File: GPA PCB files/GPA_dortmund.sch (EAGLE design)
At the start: 164 parts, among them U10 INA149SOIC8, U100 AAVID_TO220_HEATSINK, U101 AAVID_TO220_HEATSINK, U102 AAVID_TO220_HEATSINK, U103 AAVID_TO220_HEATSINK, U11 OPA549_KV_11TO-220_11, U12 OPA549_KV_11TO-220_11, U13 INA149SOIC8, U17 OPA549_KV_11TO-220_11, U18 OPA549_KV_11TO-220_11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

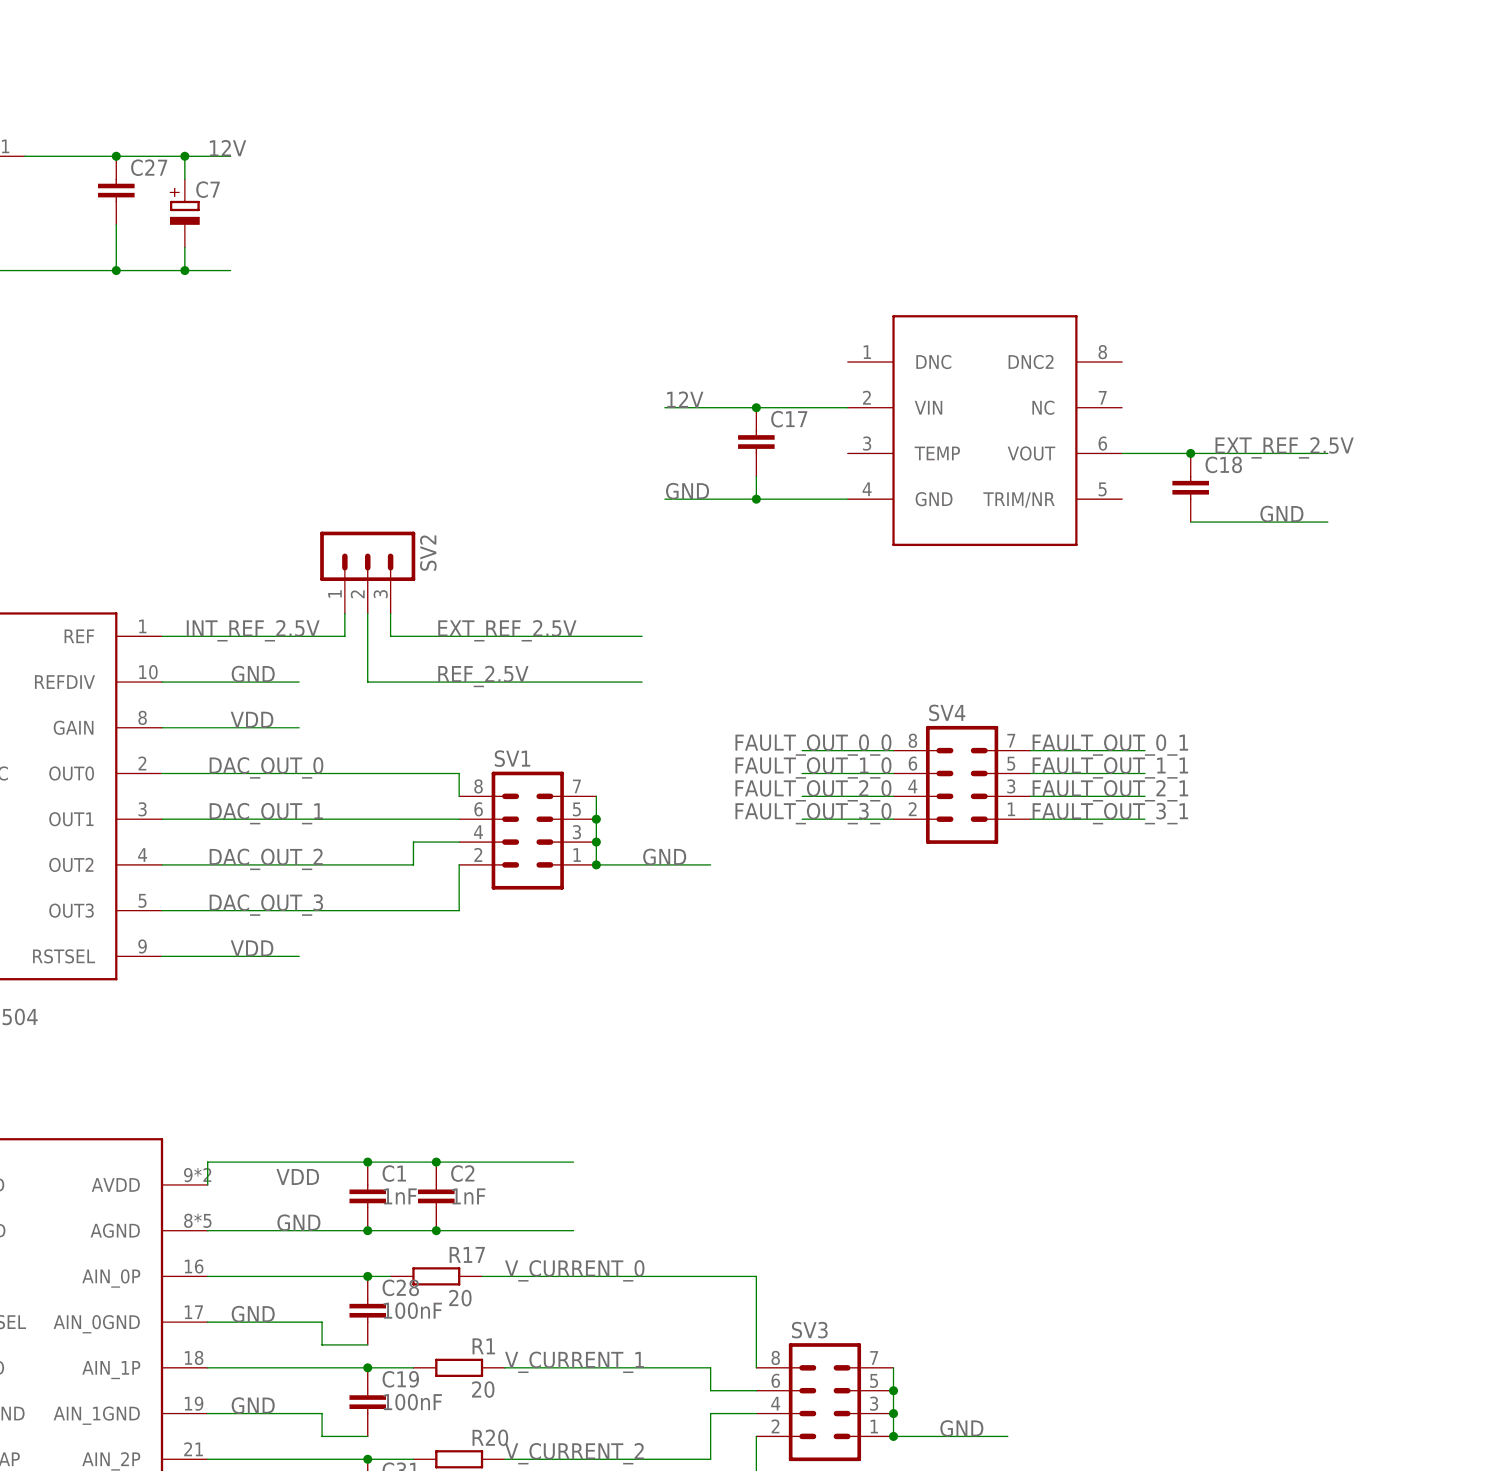
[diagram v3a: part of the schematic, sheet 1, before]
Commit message: added jumpers for switching between analog and digital input
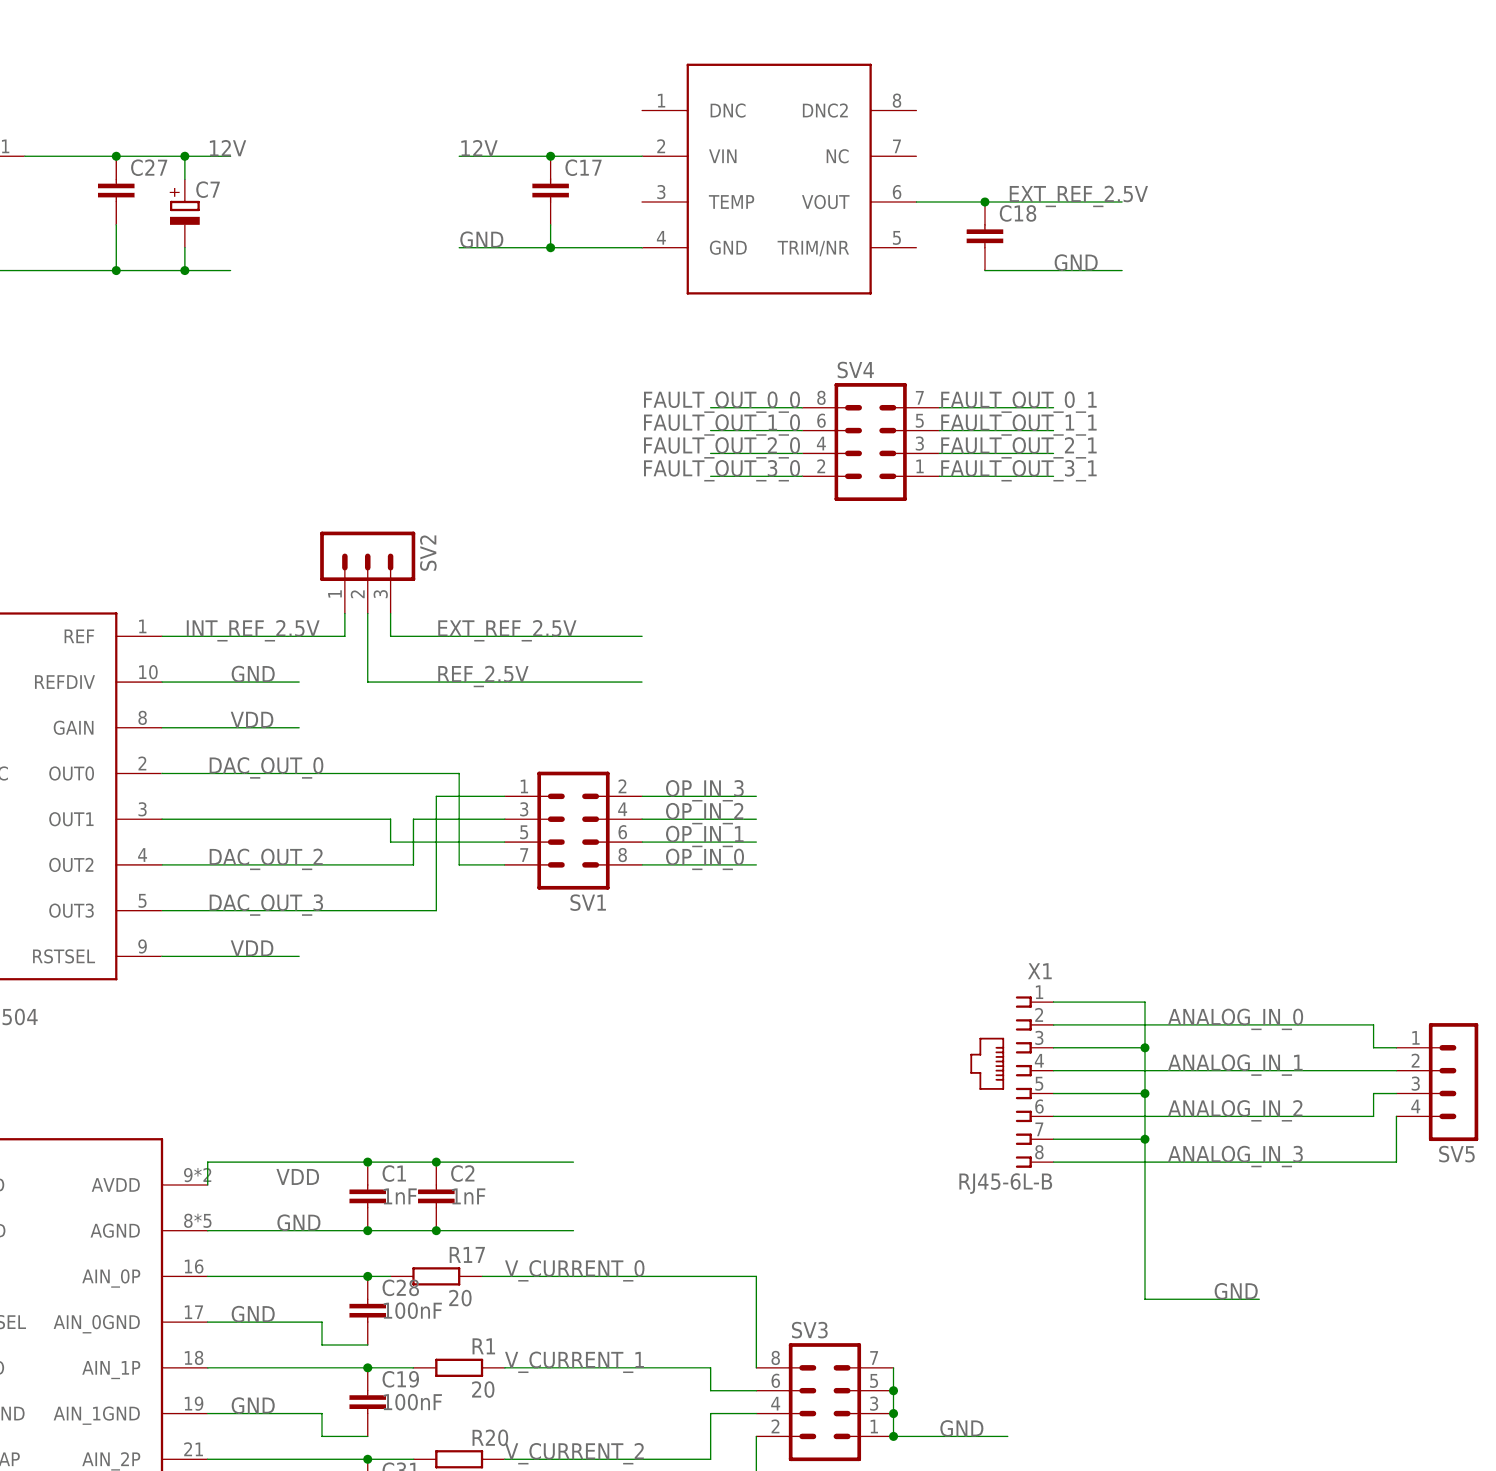
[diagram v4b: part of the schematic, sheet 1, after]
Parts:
- added SV5: (no value), my_parts:MA04-1_SLIM
- added X1: RJ45-6L-B, con-tycoelectronics:RJ45-6L-B
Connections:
- removed net DAC_OUT_1: R70.2, SV1.6, U6.OUT1
- new net ANALOG_IN_0: SV5.1, X1.2
- new net ANALOG_IN_1: SV5.2, X1.4
- new net ANALOG_IN_2: SV5.3, X1.6
- new net ANALOG_IN_3: SV5.4, X1.8
- new net N$3: SV1.5, U6.OUT1
- new net OP_IN_0: R98.2, SV1.8
- new net OP_IN_1: R70.2, SV1.6
- new net OP_IN_2: R28.2, SV1.4
- new net OP_IN_3: R42.2, SV1.2
- net DAC_OUT_0: now also SV1.7; no longer R98.2, SV1.8
- net DAC_OUT_2: now also SV1.3; no longer R28.2, SV1.4
- net DAC_OUT_3: now also SV1.1; no longer R42.2, SV1.2
- net GND: now also X1.1, X1.3, X1.5, X1.7; no longer SV1.1, SV1.3, SV1.5, SV1.7
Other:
- moved on the sheet: C17, C18, SV1, SV4

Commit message: Revert "added jumpers for switching between analog and digital input"
This reverts commit bcba1545b7b5a1e681abaa340a80f0f9e8fd90d3.
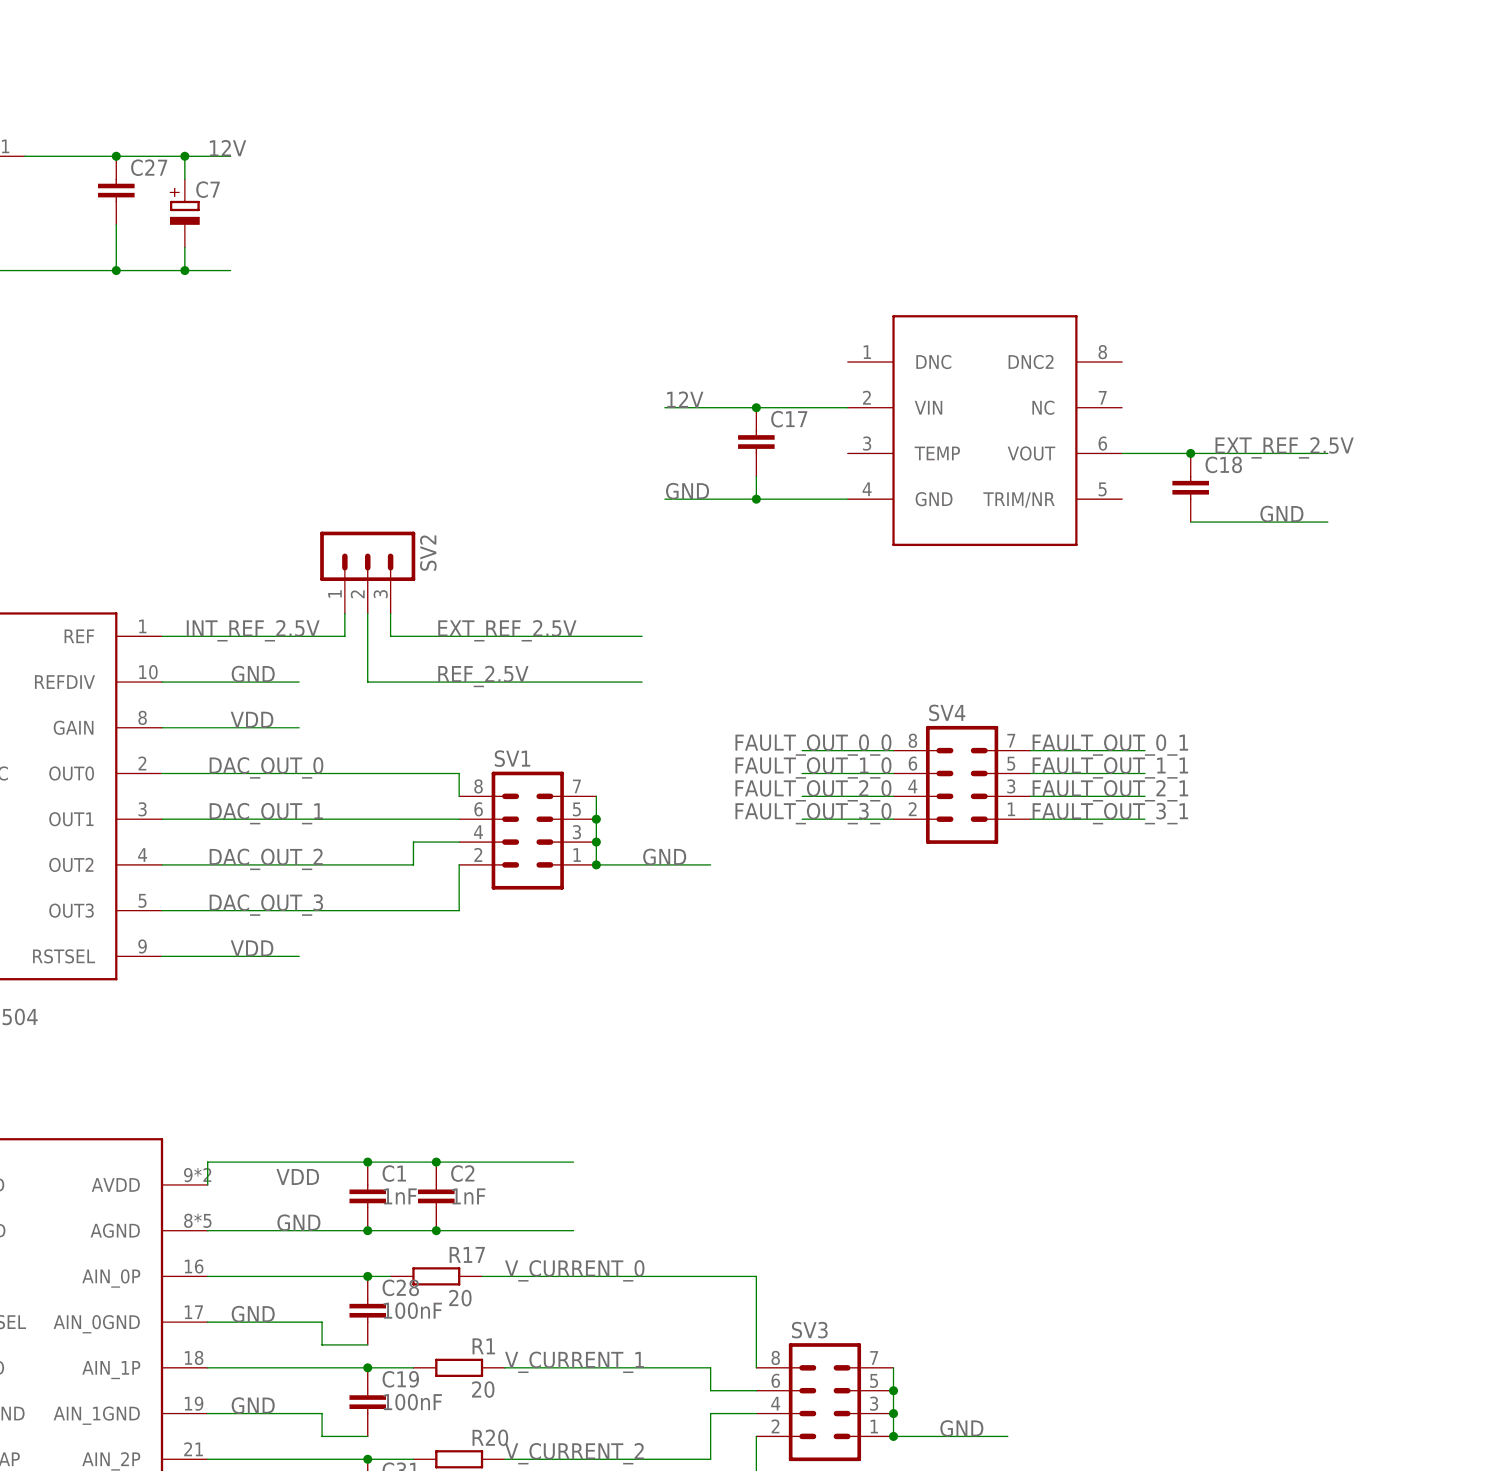
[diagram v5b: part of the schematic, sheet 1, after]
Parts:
- removed SV5: (no value), my_parts:MA04-1_SLIM
- removed X1: RJ45-6L-B, con-tycoelectronics:RJ45-6L-B
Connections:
- removed net ANALOG_IN_0: SV5.1, X1.2
- removed net ANALOG_IN_1: SV5.2, X1.4
- removed net ANALOG_IN_2: SV5.3, X1.6
- removed net ANALOG_IN_3: SV5.4, X1.8
- removed net N$3: SV1.5, U6.OUT1
- removed net OP_IN_0: R98.2, SV1.8
- removed net OP_IN_1: R70.2, SV1.6
- removed net OP_IN_2: R28.2, SV1.4
- removed net OP_IN_3: R42.2, SV1.2
- new net DAC_OUT_1: R70.2, SV1.6, U6.OUT1
- net DAC_OUT_0: now also R98.2, SV1.8; no longer SV1.7
- net DAC_OUT_2: now also R28.2, SV1.4; no longer SV1.3
- net DAC_OUT_3: now also R42.2, SV1.2; no longer SV1.1
- net GND: now also SV1.1, SV1.3, SV1.5, SV1.7; no longer X1.1, X1.3, X1.5, X1.7
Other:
- moved on the sheet: C17, C18, SV1, SV4
